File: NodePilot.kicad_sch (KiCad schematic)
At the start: 38 parts, among them K1 SRD-05VDC-SL-C, Q1 2N3904, Q2 2N3904, Q4 2N3904, T1 1:1 600R, T2 1:1 600R, U1 PC817, U2 PC817, U3 B0505S-1WR2

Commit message: NodePilot Advanced
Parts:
- removed RV3: 10k, symbol Device:R_Potentiometer_US
- Q2: value 2N3904 -> 2N2222
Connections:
- net at K1.4, R14.2, T1.5 (SA): no longer RV2.3
- net at RV2.1: now also C4.2
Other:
- title: NodePilot Remix By S21TIP -> NodePilot Advanced By S21TIP
- moved on the sheet: C1, C10, C2, C3, C4, C5, C6, C7, C8, C9, D3, K1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

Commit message: 3904 hardware config error
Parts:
- added JP1: Jumper JP1, symbol Jumper:Jumper_2_Open
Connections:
- net RIGAF: now also JP1.2 (B); no longer R1.2
- net at R14.1: now also Q1.1 (E); no longer Q1.3 (C)
- net at C9.2, U2.2: now also Q1.3 (C); no longer Q1.1 (E)
- new net EXT_COS: JP1.1 (A), R1.2
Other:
- moved on the sheet: Q1, R1
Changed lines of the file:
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@@
-	)
-	(junction
-		(at 215.9 63.5)
-		(diameter 0)
-		(color 0 0 0 0)
 	)
 	(junction
@@
 	)
 	(junction
+		(at 201.93 88.9)
+		(diameter 0)
+		(color 0 0 0 0)
+	)
+	(junction
 		(at 158.75 29.21)
 		(diameter 0)
@@
 	(junction
 		(at 144.78 118.11)
+		(diameter 0)
+		(color 0 0 0 0)
+	)
+	(junction
+		(at 201.93 63.5)
 		(diameter 0)
 		(color 0 0 0 0)
@@
 	(wire
 		(pts
+			(xy 201.93 81.28) (xy 201.93 88.9)
+		)
+		(stroke
+			(width 0)
+			(type default)
+		)
+	)
+	(wire
+		(pts
 			(xy 133.35 43.18) (xy 133.35 49.53)
 		)
@@
 	(wire
 		(pts
+			(xy 201.93 88.9) (xy 196.85 88.9)
+		)
+		(stroke
+			(width 0)
+			(type default)
+		)
+	)
+	(wire
+		(pts
 			(xy 60.96 133.35) (xy 53.34 133.35)
 		)
@@
 	(wire
 		(pts
+			(xy 201.93 63.5) (xy 201.93 71.12)
+		)
+		(stroke
+			(width 0)
+			(type default)
+		)
+	)
+	(wire
+		(pts
 			(xy 144.78 138.43) (xy 144.78 134.62)
 		)
@@
 	(wire
 		(pts
-			(xy 215.9 63.5) (xy 215.9 88.9)
-		)
-		(stroke
-			(width 0)
-			(type default)
-		)
-	)
-	(wire
-		(pts
 			(xy 144.78 134.62) (xy 161.29 134.62)
 		)
@@
 	(wire
 		(pts
+			(xy 201.93 63.5) (xy 222.25 63.5)
+		)
+		(stroke
+			(width 0)
+			(type default)
+		)
+	)
+	(wire
+		(pts
 			(xy 116.84 149.86) (xy 144.78 149.86)
 		)
@@
 	(wire
 		(pts
+			(xy 201.93 88.9) (xy 222.25 88.9)
+		)
+		(stroke
+			(width 0)
+			(type default)
+		)
+	)
+	(wire
+		(pts
 			(xy 105.41 59.69) (xy 111.76 59.69)
 		)
@@
 	(wire
 		(pts
-			(xy 203.2 88.9) (xy 215.9 88.9)
-		)
-		(stroke
-			(width 0)
-			(type default)
-		)
-	)
-	(wire
-		(pts
 			(xy 52.07 97.79) (xy 78.74 97.79)
 		)
@@
 	(wire
 		(pts
-			(xy 193.04 63.5) (xy 215.9 63.5)
+			(xy 193.04 63.5) (xy 201.93 63.5)
 		)
 		(stroke
@@
 	(wire
 		(pts
-			(xy 184.15 88.9) (xy 195.58 88.9)
+			(xy 184.15 88.9) (xy 189.23 88.9)
 		)
 		(stroke
@@
 		(pts
 			(xy 78.74 83.82) (xy 134.62 83.82)
-		)
-		(stroke
-			(width 0)
-			(type default)
-		)
-	)
-	(wire
-		(pts
-			(xy 215.9 63.5) (xy 222.25 63.5)
 		)
 		(stroke
@@
 				)
 				(justify right)
+			)
+		)
+	)
+	(global_label "EXT_COS"
+		(shape output)
+		(at 222.25 88.9 0)
+		(fields_autoplaced yes)
+		(effects
+			(font
+				(size 1.27 1.27)
+			)
+			(justify left)
+		)
+		(property "Intersheetrefs" "${INTERSHEET_REFS}"
+			(at 233.3389 88.9 0)
+			(hide yes)
+			(show_name no)
+			(do_not_autoplace no)
+			(effects
+				(font
+					(size 1.27 1.27)
+				)
+				(justify left)
 			)
 		)
@@
 	(symbol
 		(lib_id "Transistor_BJT:2N3904")
-		(at 179.07 88.9 180)
+		(at 179.07 88.9 0)
+		(mirror y)
 		(unit 1)
 		(body_style 1)
@@
 		(dnp no)
 		(property "Reference" "Q1"
-			(at 173.99 90.1701 0)
+			(at 173.99 87.6299 0)
 			(show_name no)
 			(do_not_autoplace no)
@@
 		)
 		(property "Value" "2N3904"
-			(at 173.99 87.6301 0)
+			(at 173.99 90.1699 0)
 			(show_name no)
 			(do_not_autoplace no)
@@
 		)
 		(property "Footprint" "Package_TO_SOT_THT:TO-92_Inline"
-			(at 173.99 86.995 0)
+			(at 173.99 90.805 0)
 			(hide yes)
 			(show_name no)
@@
 	(symbol
 		(lib_id "Device:R_US")
-		(at 199.39 88.9 90)
+		(at 193.04 88.9 90)
 		(unit 1)
 		(body_style 1)
@@
 		(fields_autoplaced yes)
 		(property "Reference" "R1"
-			(at 199.39 82.55 90)
+			(at 193.04 82.55 90)
 			(show_name no)
 			(do_not_autoplace no)
@@
 		)
 		(property "Value" "2.2k ohm"
-			(at 199.39 85.09 90)
+			(at 193.04 85.09 90)
 			(show_name no)
 			(do_not_autoplace no)
@@
 		)
 		(property "Footprint" ""
-			(at 199.644 87.884 90)
+			(at 193.294 87.884 90)
 			(hide yes)
 			(show_name no)
@@
 		)
 		(property "Datasheet" ""
-			(at 199.39 88.9 0)
+			(at 193.04 88.9 0)
 			(hide yes)
 			(show_name no)
@@
 		)
 		(property "Description" "Resistor, US symbol"
-			(at 199.39 88.9 0)
+			(at 193.04 88.9 0)
 			(hide yes)
 			(show_name no)
@@
 					(unit 1)
 				)
+			)
+		)
+	)
+	(symbol
+		(lib_id "Jumper:Jumper_2_Open")
+		(at 201.93 76.2 90)
+		(unit 1)
+		(body_style 1)
+		(exclude_from_sim no)
+		(in_bom yes)
+		(on_board yes)
+		(in_pos_files yes)
+		(dnp no)
+		(fields_autoplaced yes)
+		(property "Reference" "JP1"
+			(at 203.2 74.9299 90)
+			(show_name no)
+			(do_not_autoplace no)
+			(effects
+				(font
+					(size 1.27 1.27)
+				)
+				(justify right)
+			)
+		)
+		(property "Value" "Jumper JP1"
+			(at 203.2 77.4699 90)
+			(show_name no)
+			(do_not_autoplace no)
+			(effects
+				(font
+					(size 1.27 1.27)
+				)
+				(justify right)
+			)
+		)
+		(property "Footprint" ""
+			(at 201.93 76.2 0)
+			(hide yes)
+			(show_name no)
+			(do_not_autoplace no)
+			(effects
+				(font
+					(size 1.27 1.27)
+				)
+			)
+		)
+		(property "Datasheet" ""
+			(at 201.93 76.2 0)
+			(hide yes)
+			(show_name no)
+			(do_not_autoplace no)
+			(effects
+				(font
+					(size 1.27 1.27)
+				)
+			)
+		)
+		(property "Description" "Jumper, 2-pole, open"
+			(at 201.93 76.2 0)
+			(hide yes)
+			(show_name no)
+			(do_not_autoplace no)
+			(effects
+				(font
+					(size 1.27 1.27)
+				)
+			)
+		)
+		(pin "2"
+		)
+		(pin "1"
+		)
+		(instances
+			(project "NodePilot"
+				(path "/feb6dcc4-ba57-4640-ad64-1efd302ce012"
+					(reference "JP1")
+					(unit 1)
+				)

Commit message: rename
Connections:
- net EXT_COS renamed EXT_COR
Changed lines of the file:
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@@
 		)
 	)
-	(global_label "EXT_COS"
+	(global_label "EXT_COR"
 		(shape output)
 		(at 222.25 88.9 0)
@@
 		)
 		(property "Intersheetrefs" "${INTERSHEET_REFS}"
-			(at 233.3389 88.9 0)
+			(at 233.3994 88.9 0)
 			(hide yes)
 			(show_name no)

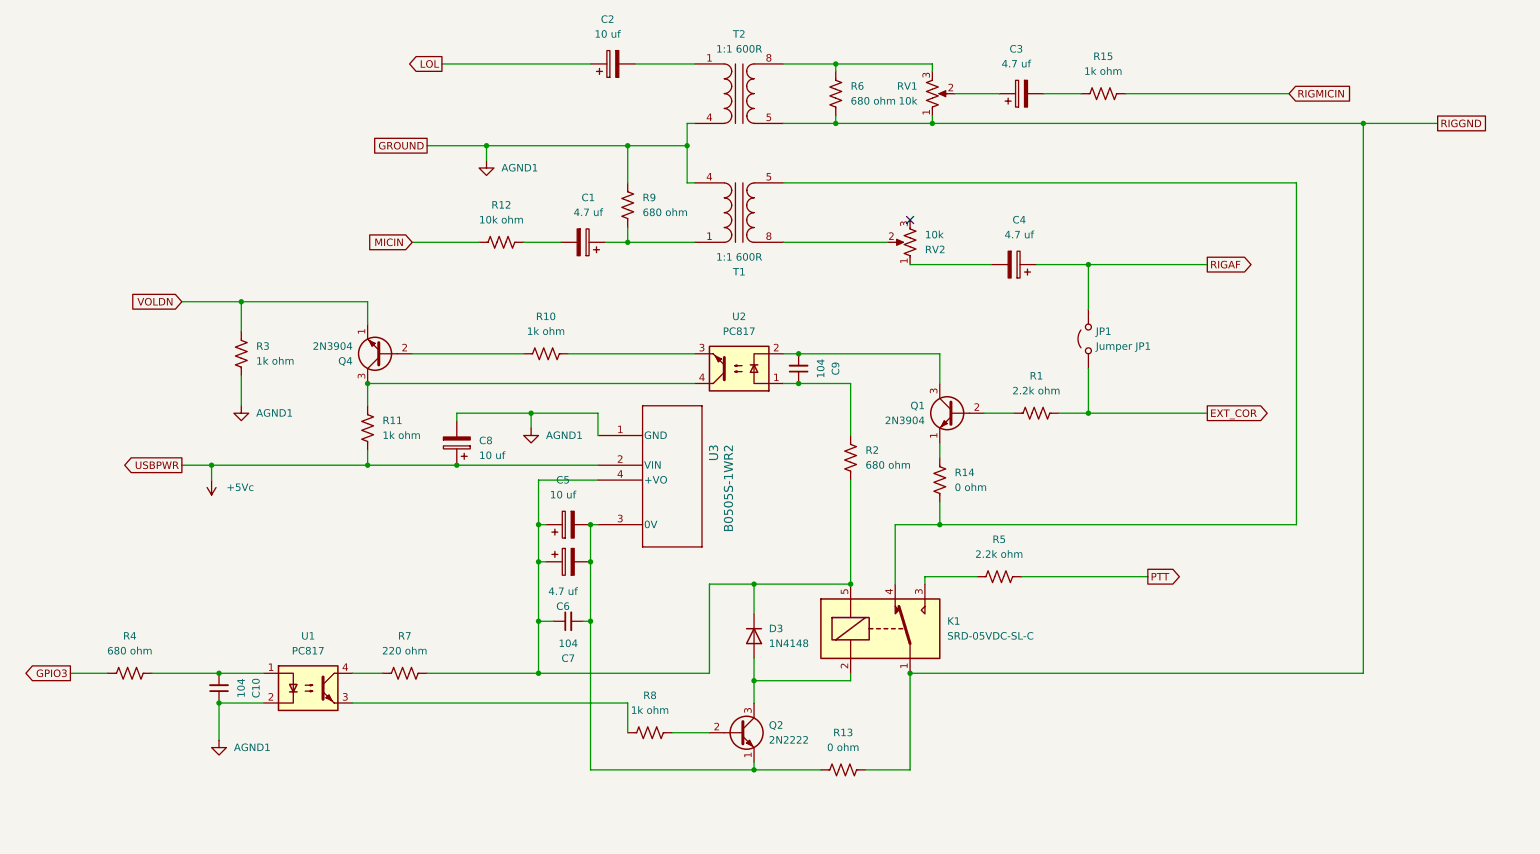
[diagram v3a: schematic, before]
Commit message: cap values for af dc blocking filtering
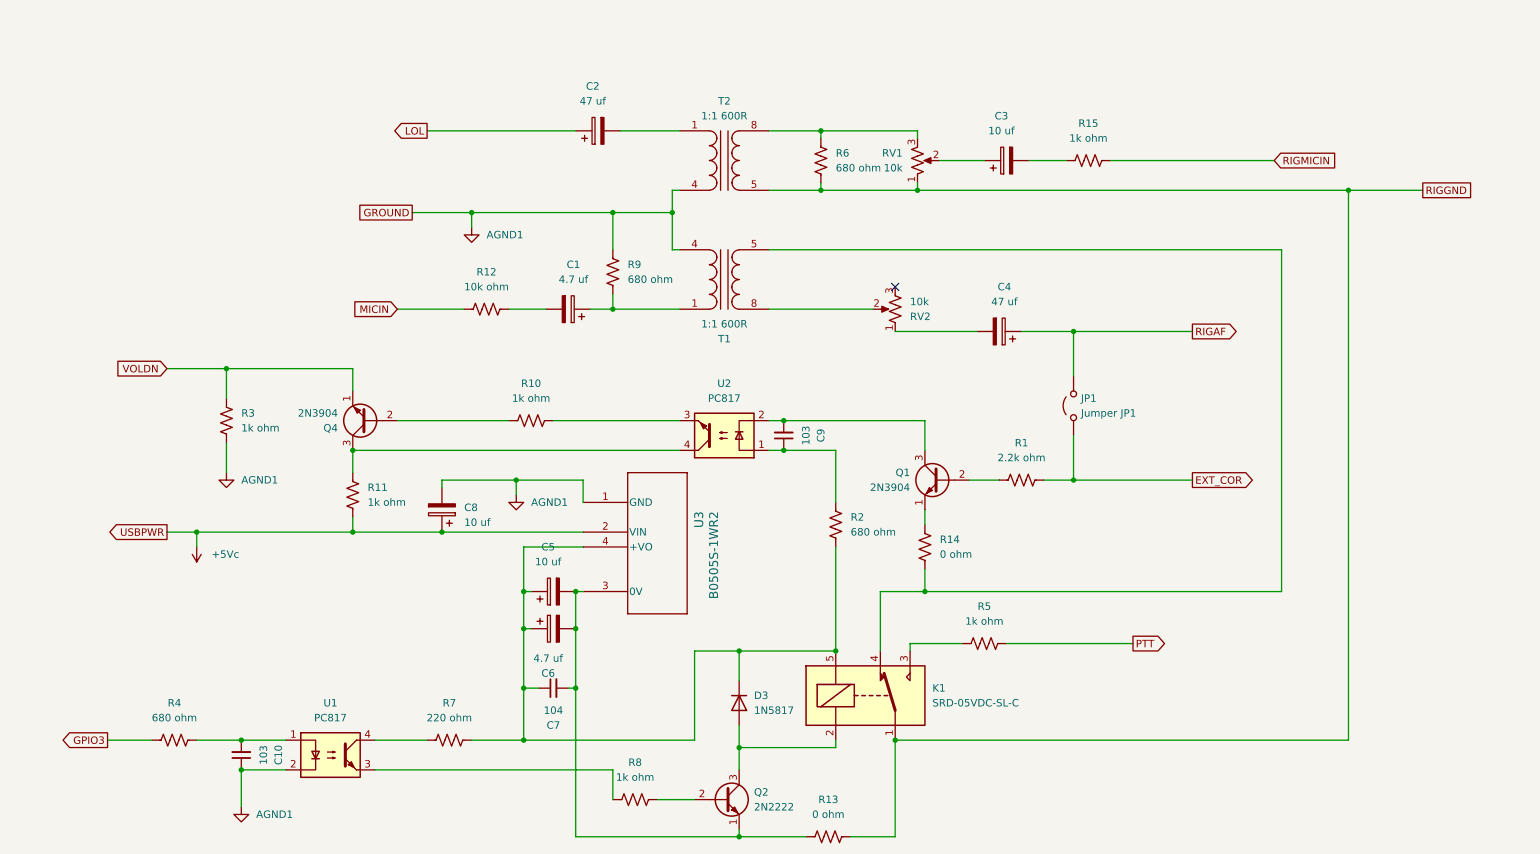
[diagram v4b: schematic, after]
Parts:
- C10, C9: value 104 -> 103
- C2: value 10 uf -> 47 uf
- C3: value 4.7 uf -> 10 uf
- C4: value 4.7 uf -> 47 uf
- D3: value 1N4148 -> 1N5817
- R5: value 2.2k ohm -> 1k ohm
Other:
- moved on the sheet: C1, C10, C2, C3, C4, C5, C6, C7, C8, C9, D3, JP1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

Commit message: big update
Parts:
- removed C9: 103, symbol Device:C_Small
- removed R14: 0 ohm, symbol Device:R_US
- added C11: 10 uf, symbol Device:C_Polarized
- added R16: 100k ohm, symbol Device:R_US
- added R17: 10k ohm, symbol Device:R_US
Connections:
- net EXT_COR: no longer JP1.1 (A)
- net RIGAF: now also R17.1; no longer JP1.2 (B)
- net at Q1.1 (E): now also K1.4, T1.5 (SA), C11.2, R16.2
- net at Q1.2 (B), R1.1: now also JP1.1 (A), C11.1, R16.1
- new net: JP1.2 (B), R17.2
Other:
- moved on the sheet: C4, JP1

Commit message: plot fix
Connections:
- net RIGAF: now also JP1.2 (B); no longer R17.1
- net at C11.1, Q1.2 (B), R1.1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: now also R17.2; no longer JP1.1 (A)
- new net: JP1.1 (A), R17.1
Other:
- moved on the sheet: JP1
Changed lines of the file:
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@@
 	)
 	(junction
-		(at 142.24 146.05)
+		(at 195.58 74.93)
 		(diameter 0)
 		(color 0 0 0 0)
 	)
 	(junction
-		(at 195.58 74.93)
+		(at 142.24 146.05)
 		(diameter 0)
 		(color 0 0 0 0)
@@
 	(wire
 		(pts
-			(xy 195.58 95.25) (xy 195.58 100.33)
+			(xy 130.81 54.61) (xy 130.81 60.96)
 		)
 		(stroke
@@
 	(wire
 		(pts
-			(xy 130.81 54.61) (xy 130.81 60.96)
+			(xy 105.41 119.38) (xy 105.41 125.73)
 		)
 		(stroke
@@
 	(wire
 		(pts
-			(xy 105.41 119.38) (xy 105.41 125.73)
+			(xy 147.32 60.96) (xy 234.95 60.96)
 		)
 		(stroke
@@
 	(wire
 		(pts
-			(xy 147.32 60.96) (xy 234.95 60.96)
+			(xy 195.58 76.2) (xy 195.58 74.93)
 		)
 		(stroke
@@
 	(wire
 		(pts
-			(xy 195.58 74.93) (xy 219.71 74.93)
-		)
-		(stroke
-			(width 0)
-			(type default)
-		)
-	)
-	(wire
-		(pts
 			(xy 120.65 54.61) (xy 120.65 60.96)
 		)
@@
 	(wire
 		(pts
-			(xy 187.96 74.93) (xy 195.58 74.93)
-		)
-		(stroke
-			(width 0)
-			(type default)
-		)
-	)
-	(wire
-		(pts
 			(xy 171.45 128.27) (xy 171.45 129.54)
 		)
@@
 	(wire
 		(pts
-			(xy 205.74 45.72) (xy 233.68 45.72)
+			(xy 195.58 74.93) (xy 219.71 74.93)
 		)
 		(stroke
@@
 	(wire
 		(pts
-			(xy 113.03 135.89) (xy 114.3 135.89)
+			(xy 205.74 45.72) (xy 233.68 45.72)
 		)
 		(stroke
@@
 	(wire
 		(pts
-			(xy 57.15 149.86) (xy 64.77 149.86)
+			(xy 113.03 135.89) (xy 114.3 135.89)
 		)
 		(stroke
@@
 	(wire
 		(pts
-			(xy 173.99 105.41) (xy 173.99 119.38)
+			(xy 57.15 149.86) (xy 64.77 149.86)
 		)
 		(stroke
@@
 	(wire
 		(pts
-			(xy 161.29 161.29) (xy 168.91 161.29)
+			(xy 173.99 105.41) (xy 173.99 119.38)
 		)
 		(stroke
@@
 	(wire
 		(pts
-			(xy 134.62 144.78) (xy 134.62 129.54)
+			(xy 161.29 161.29) (xy 168.91 161.29)
 		)
 		(stroke
@@
 	(wire
 		(pts
-			(xy 173.99 119.38) (xy 184.15 119.38)
+			(xy 134.62 144.78) (xy 134.62 129.54)
 		)
 		(stroke
@@
 	(wire
 		(pts
-			(xy 44.45 81.28) (xy 54.61 81.28)
+			(xy 173.99 119.38) (xy 184.15 119.38)
 		)
 		(stroke
@@
 	(wire
 		(pts
-			(xy 195.58 77.47) (xy 195.58 74.93)
+			(xy 44.45 81.28) (xy 54.61 81.28)
 		)
 		(stroke
@@
 	(wire
 		(pts
+			(xy 187.96 74.93) (xy 195.58 74.93)
+		)
+		(stroke
+			(width 0)
+			(type default)
+		)
+	)
+	(wire
+		(pts
 			(xy 105.41 111.76) (xy 115.57 111.76)
 		)
@@
 	(wire
 		(pts
+			(xy 195.58 96.52) (xy 195.58 100.33)
+		)
+		(stroke
+			(width 0)
+			(type default)
+		)
+	)
+	(wire
+		(pts
 			(xy 181.61 100.33) (xy 184.15 100.33)
 		)
@@
 	(wire
 		(pts
+			(xy 195.58 86.36) (xy 195.58 88.9)
+		)
+		(stroke
+			(width 0)
+			(type default)
+		)
+	)
+	(wire
+		(pts
 			(xy 54.61 93.98) (xy 54.61 99.06)
 		)
@@
 	(symbol
 		(lib_id "Jumper:Jumper_2_Open")
-		(at 195.58 90.17 90)
+		(at 195.58 81.28 90)
 		(unit 1)
 		(body_style 1)
@@
 		(fields_autoplaced yes)
 		(property "Reference" "JP1"
-			(at 196.85 88.8999 90)
+			(at 196.85 80.0099 90)
 			(show_name no)
 			(do_not_autoplace no)
@@
 		)
 		(property "Value" "Jumper JP1"
-			(at 196.85 91.4399 90)
+			(at 196.85 82.5499 90)
 			(show_name no)
 			(do_not_autoplace no)
@@
 		)
 		(property "Footprint" ""
-			(at 195.58 90.17 0)
+			(at 195.58 81.28 0)
 			(hide yes)
 			(show_name no)
@@
 		)
 		(property "Datasheet" ""
-			(at 195.58 90.17 0)
+			(at 195.58 81.28 0)
 			(hide yes)
 			(show_name no)
@@
 		)
 		(property "Description" "Jumper, 2-pole, open"
-			(at 195.58 90.17 0)
+			(at 195.58 81.28 0)
 			(hide yes)
 			(show_name no)
@@
 	)
 	(symbol
-		(lib_id "Device:R_US")
-		(at 195.58 81.28 0)
-		(unit 1)
-		(body_style 1)
-		(exclude_from_sim no)
-		(in_bom yes)
-		(on_board yes)
-		(in_pos_files yes)
-		(dnp no)
-		(property "Reference" "R17"
-			(at 198.12 80.0099 0)
-			(show_name no)
-			(do_not_autoplace no)
-			(effects
-				(font
-					(size 1.27 1.27)
-				)
-				(justify left)
-			)
-		)
-		(property "Value" "10k ohm"
-			(at 198.12 82.5499 0)
-			(show_name no)
-			(do_not_autoplace no)
-			(effects
-				(font
-					(size 1.27 1.27)
-				)
-				(justify left)
-			)
-		)
-		(property "Footprint" ""
-			(at 196.596 81.534 90)
-			(hide yes)
-			(show_name no)
-			(do_not_autoplace no)
-			(effects
-				(font
-					(size 1.27 1.27)
-				)
-			)
-		)
-		(property "Datasheet" ""
-			(at 195.58 81.28 0)
-			(hide yes)
-			(show_name no)
-			(do_not_autoplace no)
-			(effects
-				(font
-					(size 1.27 1.27)
-				)
-			)
-		)
-		(property "Description" "Resistor, US symbol"
-			(at 195.58 81.28 0)
-			(hide yes)
-			(show_name no)
-			(do_not_autoplace no)
-			(effects
-				(font
-					(size 1.27 1.27)
-				)
-			)
-		)
-		(pin "1"
-		)
-		(pin "2"
-		)
-		(instances
-			(project "NodePilot"
-				(path "/feb6dcc4-ba57-4640-ad64-1efd302ce012"
-					(reference "R17")
-					(unit 1)
-				)
-			)
-		)
-	)
-	(symbol
 		(lib_id "Device:C_Polarized")
 		(at 187.96 45.72 90)
@@
 					(unit 1)
 				)
+			)
+		)
+	)
+	(symbol
+		(lib_id "Device:R_US")
+		(at 195.58 92.71 0)
+		(unit 1)
+		(body_style 1)
+		(exclude_from_sim no)
+		(in_bom yes)
+		(on_board yes)
+		(in_pos_files yes)
+		(dnp no)
+		(property "Reference" "R17"
+			(at 198.12 91.4399 0)
+			(show_name no)
+			(do_not_autoplace no)
+			(effects
+				(font
+					(size 1.27 1.27)
+				)
+				(justify left)
+			)
+		)
+		(property "Value" "10k ohm"
+			(at 198.12 93.9799 0)
+			(show_name no)
+			(do_not_autoplace no)
+			(effects
+				(font
+					(size 1.27 1.27)
+				)
+				(justify left)
+			)
+		)
+		(property "Footprint" ""
+			(at 196.596 92.964 90)
+			(hide yes)
+			(show_name no)
+			(do_not_autoplace no)
+			(effects
+				(font
+					(size 1.27 1.27)
+				)
+			)
+		)
+		(property "Datasheet" ""
+			(at 195.58 92.71 0)
+			(hide yes)
+			(show_name no)
+			(do_not_autoplace no)
+			(effects
+				(font
+					(size 1.27 1.27)
+				)
+			)
+		)
+		(property "Description" "Resistor, US symbol"
+			(at 195.58 92.71 0)
+			(hide yes)
+			(show_name no)
+			(do_not_autoplace no)
+			(effects
+				(font
+					(size 1.27 1.27)
+				)
+			)
+		)
+		(pin "1"
+		)
+		(pin "2"
+		)
+		(instances
+			(project "NodePilot"
+				(path "/feb6dcc4-ba57-4640-ad64-1efd302ce012"
+					(reference "R17")
+					(unit 1)
+				)

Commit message: small change in revert
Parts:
- C2: value 47 uf -> 10 uf
- C3: value 10 uf -> 4.7 uf
- C4: value 47 uf -> 4.7 uf
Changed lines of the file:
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@@
 			)
 		)
-		(property "Value" "47 uf"
+		(property "Value" "10 uf"
 			(at 117.221 35.56 90)
 			(show_name no)
@@
 			)
 		)
-		(property "Value" "10 uf"
+		(property "Value" "4.7 uf"
 			(at 187.071 40.64 90)
 			(show_name no)
@@
 			)
 		)
-		(property "Value" "47 uf"
+		(property "Value" "4.7 uf"
 			(at 185.039 69.85 90)
 			(show_name no)
